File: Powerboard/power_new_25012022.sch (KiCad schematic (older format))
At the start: 14 parts

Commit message: 13/02/2022
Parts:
- removed Q?: Q_PNP_BCE, symbol Device:Q_PNP_BCE
- removed Q?: Q_NPN_BCE, symbol Device:Q_NPN_BCE
- added C? (x2): C_Small, symbol Device:C_Small
- added J?: Conn_01x05_Male, symbol Connector:Conn_01x05_Male
- added TP? (x14): TestPoint, symbol Connector:TestPoint
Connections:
- net labels added: +24V
- wire segments 51 -> 73
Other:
- moved on the sheet: D?, P?, Q?, R?, U?

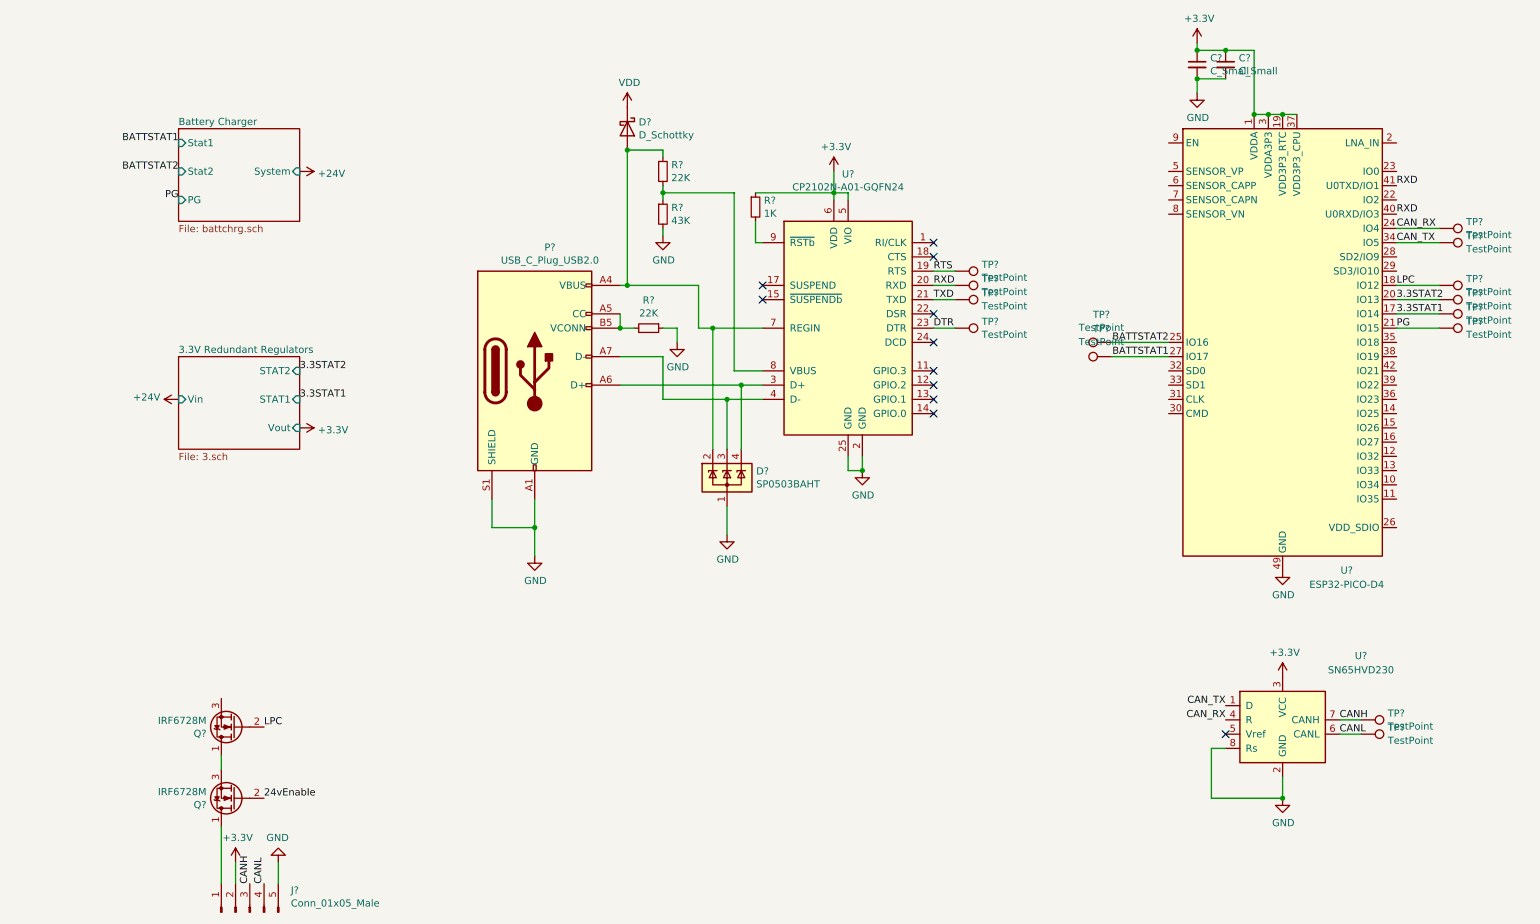
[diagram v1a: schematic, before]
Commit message: added lpc/24 enable
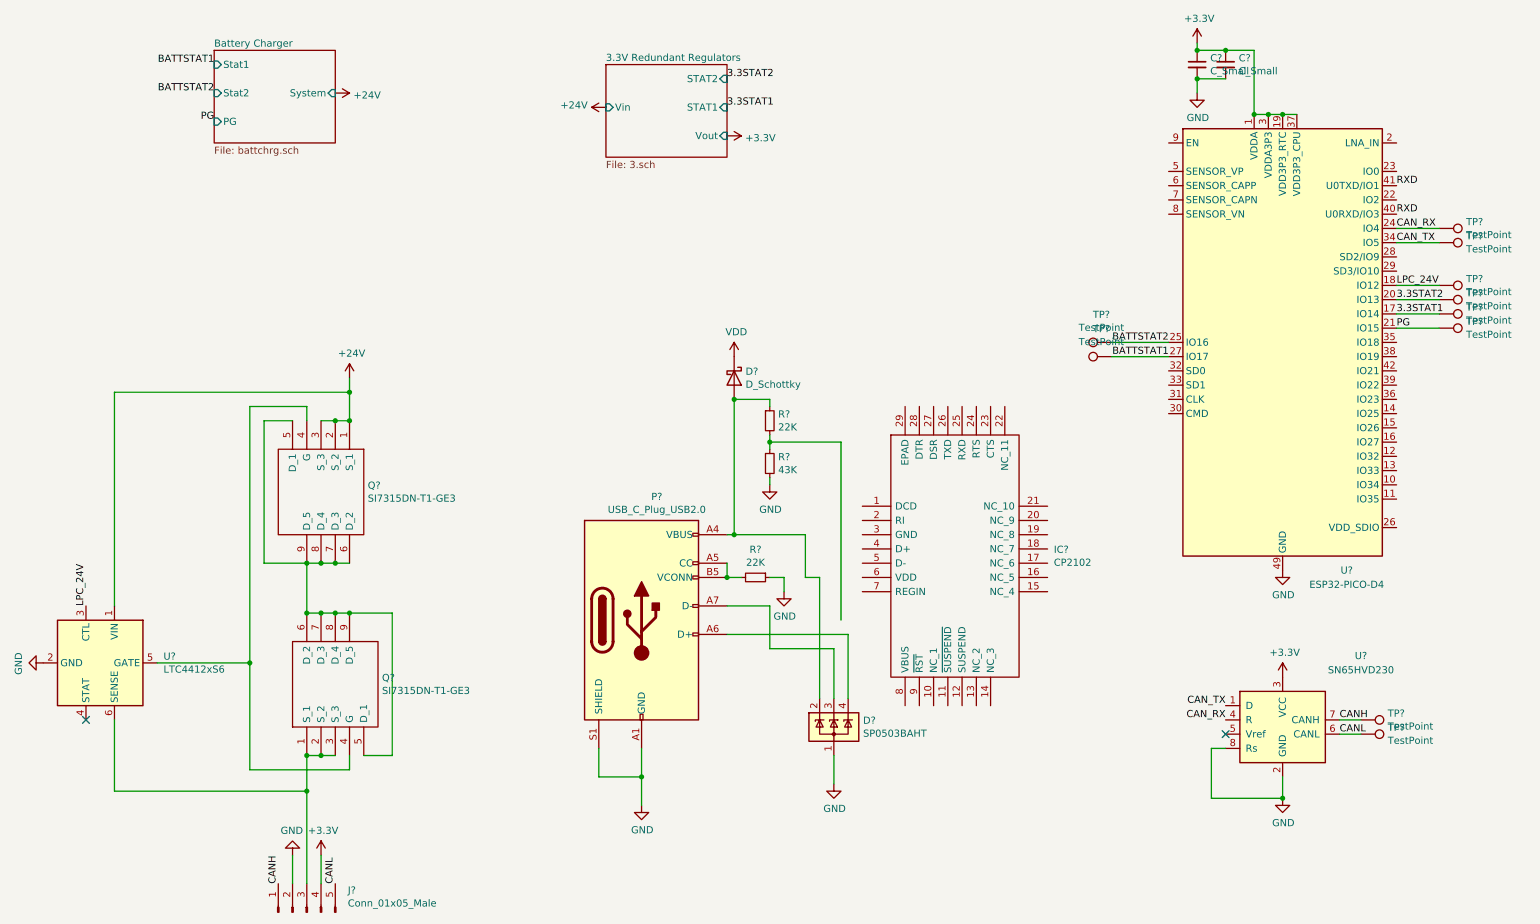
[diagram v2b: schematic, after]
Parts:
- removed Q? (x2): IRF6728M, Package_DirectFET:DirectFET_MX, symbol Transistor_FET:IRF6728M
- removed R?: 1K, symbol Device:R_Small
- removed TP? (x4): TestPoint, symbol Connector:TestPoint
- removed U?: CP2102N-A01-GQFN24, Package_DFN_QFN:QFN-24-1EP_4x4mm_P0.5mm_EP2.6x2.6mm, symbol Interface_USB:CP2102N-A01-GQFN24
- added IC?: CP2102, QFN50P500X500X100-29N-D, symbol iclr:CP2102
- added Q? (x2): SI7315DN-T1-GE3, SI7315DNT1GE3, symbol iclr:SI7315DN-T1-GE3
- added U?: LTC4412xS6, Package_TO_SOT_SMD:TSOT-23-6, symbol Power_Management:LTC4412xS6
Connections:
- net +24V: now also Q?.1 (S_1), Q?.2 (S_2), Q?.3 (S_3), U?.1 (VIN)
- net +3V3: now also J?.4 (Pin_4); no longer J?.2 (Pin_2)
- net CANH: now also J?.1 (Pin_1); no longer J?.3 (Pin_3)
- net CANL: now also J?.5 (Pin_5); no longer J?.4 (Pin_4)
- net GND: now also J?.2 (Pin_2), U?.2 (GND); no longer J?.5 (Pin_5)
- net LPC renamed LPC_24V
- net LPC_24V: now also U?.3 (CTL)
- new net: J?.3 (Pin_3), Q?.1 (S_1), Q?.2 (S_2), Q?.3 (S_3), U?.6 (SENSE)
- new net: Q?.4 (G), Q?.4 (G), U?.5 (GATE)
- new net: Q?.5 (D_1), Q?.5 (D_1), Q?.6 (D_2), Q?.6 (D_2), Q?.7 (D_3), Q?.7 (D_3), Q?.8 (D_4), Q?.8 (D_4), Q?.9 (D_5), Q?.9 (D_5)
- no-connect marks 11 -> 2
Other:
- moved on the sheet: D?, J?, P?, R?

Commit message: 19/02/2022
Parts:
- removed D?: SP0503BAHT, Package_TO_SOT_SMD:SOT-143, symbol Power_Protection:SP0503BAHT
- removed D?: D_Schottky, symbol Device:D_Schottky
- removed P?: USB_C_Plug_USB2.0, symbol Connector:USB_C_Plug_USB2.0
- removed R? (x2): 22K, symbol Device:R_Small
- removed R?: 43K, symbol Device:R_Small
- added C? (x4): C_Small, symbol Device:C_Small
- added D?: SP0503BAHT, Package_TO_SOT_SMD:SOT-143, symbol Power_Protection:SP0503BAHT
- added J?: USB_C_Receptacle_USB2.0, symbol Connector:USB_C_Receptacle_USB2.0
- added R? (x5): R_Small, symbol Device:R_Small
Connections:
- net +3V3: now also IC?.6 (VDD), IC?.7 (REGIN), C?.1, C?.1, C?.2, C?.2, R?.1
- net GND: now also IC?.3 (GND), C?.1, C?.1, C?.2, C?.2, R?.1, R?.1, R?.1
- net RXD: now also IC?.25 (RXD)
- net RTS: now reaches IC?.24 (RTS)
- net TXD: now reaches IC?.26 (TXD)
- net DTR: now reaches IC?.28 (DTR)
- net at IC?.4 (D+): now also D?.4 (K), J?.A6 (D+), J?.B6 (D+)
- net at IC?.5 (D-): now also D?.3 (K), J?.A7 (D-), J?.B7 (D-)
- net at IC?.8 (VBUS): now also R?.2, R?.2
- net at IC?.9 (~RST): now also R?.2
- new net: J?.A1 (GND), J?.A12 (GND), J?.B1 (GND), J?.B12 (GND)
- new net: J?.A5 (CC1), R?.2
- new net: J?.B5 (CC2), R?.2
- new net VBUS: D?.2 (K), J?.A4 (VBUS), J?.A9 (VBUS), J?.B4 (VBUS), J?.B9 (VBUS), R?.1
- no-connect marks 2 -> 21
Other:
- moved on the sheet: IC?
